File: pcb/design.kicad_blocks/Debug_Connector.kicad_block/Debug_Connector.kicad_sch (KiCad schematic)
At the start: 1 part, among them J2 Debug

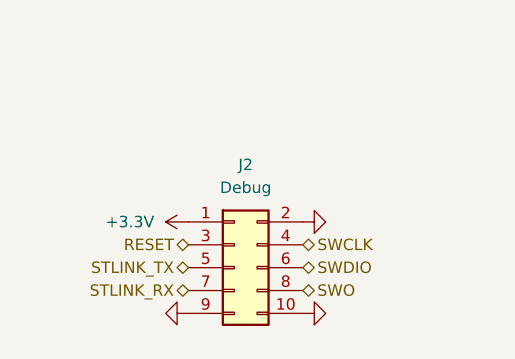
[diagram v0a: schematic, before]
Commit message: Trying out design blocks instead of hierarchal sheets.
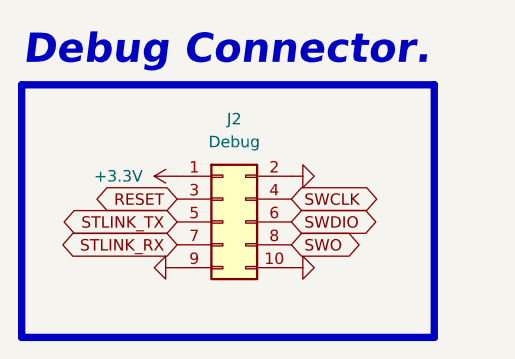
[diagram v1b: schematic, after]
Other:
- note added: "Debug Connector."
- moved on the sheet: J2
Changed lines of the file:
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@@
 	(generator_version "9.0")
 	(paper "A5")
-	(hierarchical_label "SWDIO"
-		(shape bidirectional)
-		(at 111.76 71.12 0)
+	(rectangle
+		(start 80.518 50.8)
+		(end 126.365 78.867)
+		(stroke
+			(width 0.8128)
+			(type solid)
+			(color 255 0 0 1)
+		)
+		(fill
+			(type none)
+		)
+	)
+	(text "Debug Connector."
+		(exclude_from_sim no)
+		(at 80.645 48.895 0)
+		(effects
+			(font
+				(size 3.2512 3.2512)
+				(thickness 0.6502)
+				(bold yes)
+				(italic yes)
+				(color 255 0 0 1)
+			)
+			(justify left bottom)
+		)
+	)
+	(global_label "SWO"
+		(shape bidirectional)
+		(at 110.49 68.58 0)
+		(fields_autoplaced yes)
 		(effects
 			(font
@@
 			(justify left)
 		)
-	)
-	(hierarchical_label "SWCLK"
-		(shape bidirectional)
-		(at 111.76 68.58 0)
+		(property "Intersheetrefs" "${INTERSHEET_REFS}"
+			(at 118.5779 68.58 0)
+			(effects
+				(font
+					(size 1.27 1.27)
+				)
+				(justify left)
+				(hide yes)
+			)
+		)
+	)
+	(global_label "RESET"
+		(shape bidirectional)
+		(at 97.79 63.5 180)
+		(fields_autoplaced yes)
+		(effects
+			(font
+				(size 1.27 1.27)
+			)
+			(justify right)
+		)
+		(property "Intersheetrefs" "${INTERSHEET_REFS}"
+			(at 87.9484 63.5 0)
+			(effects
+				(font
+					(size 1.27 1.27)
+				)
+				(justify right)
+				(hide yes)
+			)
+		)
+	)
+	(global_label "SWCLK"
+		(shape bidirectional)
+		(at 110.49 63.5 0)
+		(fields_autoplaced yes)
 		(effects
 			(font
@@
 			(justify left)
 		)
-	)
-	(hierarchical_label "STLINK_RX"
-		(shape bidirectional)
-		(at 99.06 73.66 180)
+		(property "Intersheetrefs" "${INTERSHEET_REFS}"
+			(at 120.8155 63.5 0)
+			(effects
+				(font
+					(size 1.27 1.27)
+				)
+				(justify left)
+				(hide yes)
+			)
+		)
+	)
+	(global_label "STLINK_TX"
+		(shape bidirectional)
+		(at 97.79 66.04 180)
+		(fields_autoplaced yes)
 		(effects
 			(font
@@
 			(justify right)
 		)
-	)
-	(hierarchical_label "STLINK_TX"
-		(shape bidirectional)
-		(at 99.06 71.12 180)
+		(property "Intersheetrefs" "${INTERSHEET_REFS}"
+			(at 84.1383 66.04 0)
+			(effects
+				(font
+					(size 1.27 1.27)
+				)
+				(justify right)
+				(hide yes)
+			)
+		)
+	)
+	(global_label "SWDIO"
+		(shape bidirectional)
+		(at 110.49 66.04 0)
+		(fields_autoplaced yes)
+		(effects
+			(font
+				(size 1.27 1.27)
+			)
+			(justify left)
+		)
+		(property "Intersheetrefs" "${INTERSHEET_REFS}"
+			(at 120.4527 66.04 0)
+			(effects
+				(font
+					(size 1.27 1.27)
+				)
+				(justify left)
+				(hide yes)
+			)
+		)
+	)
+	(global_label "STLINK_RX"
+		(shape bidirectional)
+		(at 97.79 68.58 180)
+		(fields_autoplaced yes)
 		(effects
 			(font
@@
 			(justify right)
 		)
-	)
-	(hierarchical_label "RESET"
-		(shape bidirectional)
-		(at 99.06 68.58 180)
-		(effects
-			(font
-				(size 1.27 1.27)
-			)
-			(justify right)
-		)
-	)
-	(hierarchical_label "SWO"
-		(shape bidirectional)
-		(at 111.76 73.66 0)
-		(effects
-			(font
-				(size 1.27 1.27)
-			)
-			(justify left)
+		(property "Intersheetrefs" "${INTERSHEET_REFS}"
+			(at 83.8359 68.58 0)
+			(effects
+				(font
+					(size 1.27 1.27)
+				)
+				(justify right)
+				(hide yes)
+			)
 		)
 	)
 	(symbol
 		(lib_id "power:+3.3V")
-		(at 99.06 66.04 90)
+		(at 97.79 60.96 90)
 		(unit 1)
 		(exclude_from_sim no)
@@
 		(fields_autoplaced yes)
 		(property "Reference" "#PWR018"
-			(at 102.87 66.04 0)
+			(at 101.6 60.96 0)
 			(effects
 				(font
@@
 		)
 		(property "Value" "+3.3V"
-			(at 95.25 66.0399 90)
+			(at 93.98 60.9599 90)
 			(effects
 				(font
@@
 		)
 		(property "Footprint" ""
-			(at 99.06 66.04 0)
+			(at 97.79 60.96 0)
 			(effects
 				(font
@@
 		)
 		(property "Datasheet" ""
-			(at 99.06 66.04 0)
+			(at 97.79 60.96 0)
 			(effects
 				(font
@@
 		)
 		(property "Description" "Power symbol creates a global label with name \"+3.3V\""
-			(at 99.06 66.04 0)
+			(at 97.79 60.96 0)
 			(effects
 				(font
@@
 	(symbol
 		(lib_id "power:GND")
-		(at 111.76 76.2 90)
+		(at 110.49 71.12 90)
 		(unit 1)
 		(exclude_from_sim no)
@@
 		(fields_autoplaced yes)
 		(property "Reference" "#PWR017"
-			(at 118.11 76.2 0)
+			(at 116.84 71.12 0)
 			(effects
 				(font
@@
 		)
 		(property "Value" "GND"
-			(at 115.57 76.1999 90)
+			(at 114.3 71.1199 90)
 			(effects
 				(font
@@
 		)
 		(property "Footprint" ""
-			(at 111.76 76.2 0)
+			(at 110.49 71.12 0)
 			(effects
 				(font
@@
 		)
 		(property "Datasheet" ""
-			(at 111.76 76.2 0)
+			(at 110.49 71.12 0)
 			(effects
 				(font
@@
 		)
 		(property "Description" "Power symbol creates a global label with name \"GND\" , ground"
-			(at 111.76 76.2 0)
+			(at 110.49 71.12 0)
 			(effects
 				(font
@@
 	(symbol
 		(lib_id "Connector_Generic:Conn_02x05_Odd_Even")
-		(at 104.14 71.12 0)
+		(at 102.87 66.04 0)
 		(unit 1)
 		(exclude_from_sim no)
@@
 		(fields_autoplaced yes)
 		(property "Reference" "J2"
-			(at 105.41 59.69 0)
+			(at 104.14 54.61 0)
 			(effects
 				(font
@@
 		)
 		(property "Value" "Debug"
-			(at 105.41 62.23 0)
+			(at 104.14 57.15 0)
 			(effects
 				(font
@@
 		)
 		(property "Footprint" "pcb:Molex_PicoBlade_53047-1010_1x10_P1.25mm_Vertical"
-			(at 104.14 71.12 0)
+			(at 102.87 66.04 0)
 			(effects
 				(font
@@
 		)
 		(property "Datasheet" "~"
-			(at 104.14 71.12 0)
+			(at 102.87 66.04 0)
 			(effects
 				(font
@@
 		)
 		(property "Description" "Generic connector, double row, 02x05, odd/even pin numbering scheme (row 1 odd numbers, row 2 even numbers), script generated (kicad-library-utils/schlib/autogen/connector/)"
-			(at 104.14 71.12 0)
+			(at 102.87 66.04 0)
 			(effects
 				(font
@@
 	(symbol
 		(lib_id "power:GND")
-		(at 99.06 76.2 270)
+		(at 97.79 71.12 270)
 		(unit 1)
 		(exclude_from_sim no)
@@
 		(fields_autoplaced yes)
 		(property "Reference" "#PWR019"
-			(at 92.71 76.2 0)
+			(at 91.44 71.12 0)
 			(effects
 				(font
@@
 		)
 		(property "Value" "GND"
-			(at 95.25 76.2001 90)
+			(at 93.98 71.1201 90)
 			(effects
 				(font
@@
 		)
 		(property "Footprint" ""
-			(at 99.06 76.2 0)
+			(at 97.79 71.12 0)
 			(effects
 				(font
@@
 		)
 		(property "Datasheet" ""
-			(at 99.06 76.2 0)
+			(at 97.79 71.12 0)
 			(effects
 				(font
@@
 		)
 		(property "Description" "Power symbol creates a global label with name \"GND\" , ground"
-			(at 99.06 76.2 0)
+			(at 97.79 71.12 0)
 			(effects
 				(font
@@
 	(symbol
 		(lib_id "power:GND")
-		(at 111.76 66.04 90)
+		(at 110.49 60.96 90)
 		(unit 1)
 		(exclude_from_sim no)
@@
 		(fields_autoplaced yes)
 		(property "Reference" "#PWR020"
-			(at 118.11 66.04 0)
+			(at 116.84 60.96 0)
 			(effects
 				(font
@@
 		)
 		(property "Value" "GND"
-			(at 115.57 66.0399 90)
+			(at 114.3 60.9599 90)
 			(effects
 				(font
@@
 		)
 		(property "Footprint" ""
-			(at 111.76 66.04 0)
+			(at 110.49 60.96 0)
 			(effects
 				(font
@@
 		)
 		(property "Datasheet" ""
-			(at 111.76 66.04 0)
+			(at 110.49 60.96 0)
 			(effects
 				(font
@@
 		)
 		(property "Description" "Power symbol creates a global label with name \"GND\" , ground"
-			(at 111.76 66.04 0)
-			(effects
-				(font
+			(at 110.49 60.96 0)
+			(effects
+				(font

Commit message: Updated debug connector symbol from 02x05 to 01x10.
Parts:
- removed J2: Debug, pcb:Molex_PicoBlade_53047-1010_1x10_P1.25mm_Vertical, symbol Connector_Generic:Conn_02x05_Odd_Even
- added J5: Debug, pcb:Molex_PicoBlade_53047-1010_1x10_P1.25mm_Vertical, symbol Connector_Generic:Conn_01x10
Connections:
- net +3.3V: now also J5.1 (Pin_1)
- net GND: now also J5.10 (Pin_10), J5.5 (Pin_5), J5.6 (Pin_6)
- net RESET: now also J5.2 (Pin_2)
- net STLINK_RX: now also J5.4 (Pin_4)
- net STLINK_TX: now also J5.3 (Pin_3)
- net SWCLK: now also J5.7 (Pin_7)
- net SWDIO: now also J5.8 (Pin_8)
- net SWO: now also J5.9 (Pin_9)
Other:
- note added: "TODO: If space allows, it'd be really nice to use an IDC connector instead for the debug stuff."
